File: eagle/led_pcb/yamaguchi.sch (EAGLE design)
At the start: 8 parts

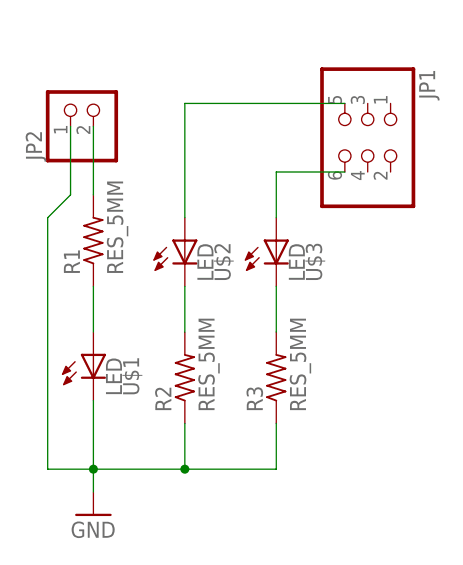
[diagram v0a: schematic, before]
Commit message: led基板の配線の修正
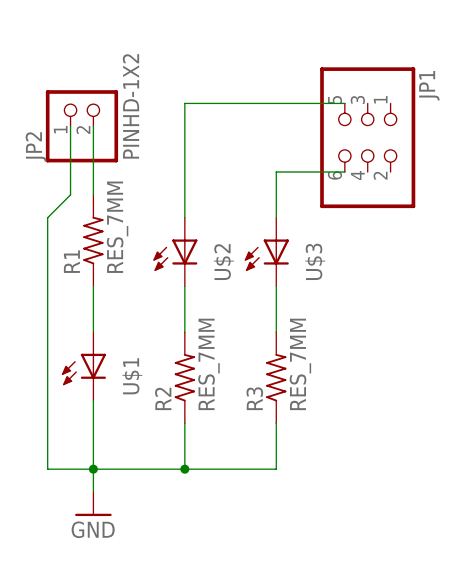
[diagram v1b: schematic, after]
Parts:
- JP2: value (none) -> PINHD-1X2; device pinhead:PINHD-1X2 -> Yamaguchi:PINHD-1X2
- R1, R2, R3: value RES_5MM -> RES_7MM; device Yamaguchi:RES_5MM -> Yamaguchi:RES_7MM
- U$1, U$2, U$3: value LED -> (none); device Yamaguchi:LED -> 01_EasyAccessLib:LED1206
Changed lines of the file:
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@@
 </classes>
 <parts>
-<part name="U$1" library="Yamaguchi" deviceset="LED" device=""/>
-<part name="U$2" library="Yamaguchi" deviceset="LED" device=""/>
-<part name="U$3" library="Yamaguchi" deviceset="LED" device=""/>
-<part name="R1" library="Yamaguchi" deviceset="RES_5MM" device=""/>
-<part name="R2" library="Yamaguchi" deviceset="RES_5MM" device=""/>
-<part name="R3" library="Yamaguchi" deviceset="RES_5MM" device=""/>
+<part name="U$1" library="01_EasyAccessLib" deviceset="LED" device="1206"/>
+<part name="U$2" library="01_EasyAccessLib" deviceset="LED" device="1206"/>
+<part name="U$3" library="01_EasyAccessLib" deviceset="LED" device="1206"/>
+<part name="R1" library="Yamaguchi" deviceset="RES_7MM" device=""/>
+<part name="R2" library="Yamaguchi" deviceset="RES_7MM" device=""/>
+<part name="R3" library="Yamaguchi" deviceset="RES_7MM" device=""/>
 <part name="JP1" library="01_EasyAccessLib" deviceset="PINHD-2X3" device=""/>
-<part name="JP2" library="pinhead" deviceset="PINHD-1X2" device=""/>
+<part name="JP2" library="Yamaguchi" deviceset="PINHD-1X2" device=""/>
 <part name="GND1" library="01_EasyAccessLib" deviceset="GND" device=""/>
 </parts>
